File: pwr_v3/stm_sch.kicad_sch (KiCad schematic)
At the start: 2 parts, among them CN11 Conn_02x36_Odd_Even, CN12 Conn_02x36_Odd_Even

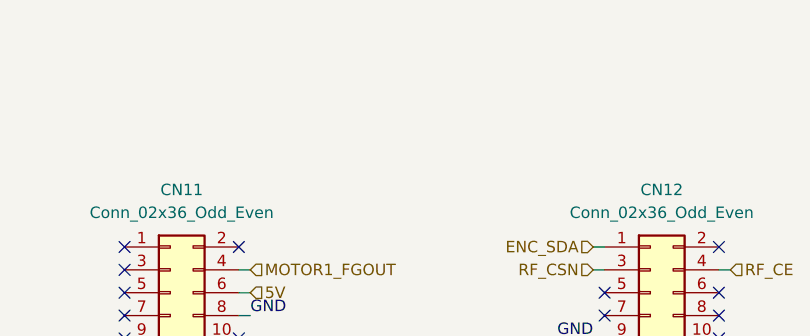
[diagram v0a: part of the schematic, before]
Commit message: Schematic and layout updated
Sch - Unwanted global labels removed from IMU, added new kicker labels, changed kicker connector footprint.
Layout - Updated kicker and encoder positions, routing updated.
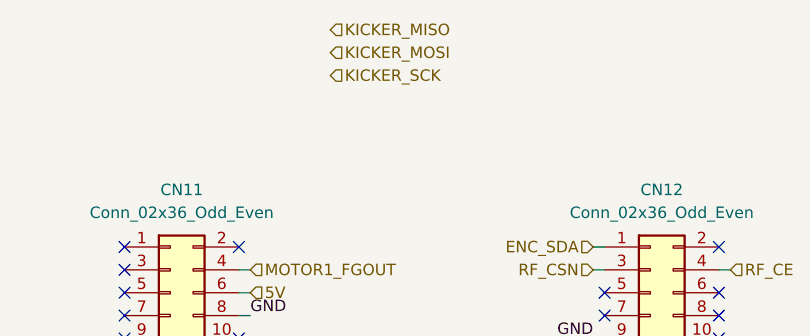
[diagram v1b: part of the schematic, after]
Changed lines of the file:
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@@
+		)
+	)
+	(hierarchical_label "KICKER_SCK"
+		(shape input)
+		(at 69.85 33.02 0)
+		(effects
+			(font
+				(size 1.27 1.27)
+			)
+			(justify left)
 		)
 	)
@@
 		)
 	)
+	(hierarchical_label "KICKER_MOSI"
+		(shape input)
+		(at 69.85 30.48 0)
+		(effects
+			(font
+				(size 1.27 1.27)
+			)
+			(justify left)
+		)
+	)
 	(hierarchical_label "RF_CSN"
 		(shape input)
@@
 		(effects
 			(font
+				(size 1.27 1.27)
+			)
+			(justify left)
+		)
+	)
+	(hierarchical_label "KICKER_MISO"
+		(shape input)
+		(at 69.85 27.94 0)
+		(effects
+			(font

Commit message: Finalized files
Final files used for fabrication. Docs and Images added for easy view.
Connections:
- net KICKER_MISO: now also CN11.54 (Pin_54)
- net KICKER_MOSI: now also CN11.56 (Pin_56)
- net KICKER_SCK: now also CN11.11 (Pin_11)
- no-connect marks 98 -> 95
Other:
- note removed: "Pin connection details"
- moved on the sheet: CN11, CN12
